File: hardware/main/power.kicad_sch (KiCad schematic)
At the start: 34 parts, among them Q1 SSM3J338R, Q10 SSM3J338R, Q2 BCP53, Q3 SSM3J338R, Q4 BC817, Q5 SSM3J338R, Q6 BC807, Q7 BC817, Q8 SSM3J338R, U5 AP2114H-3.3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

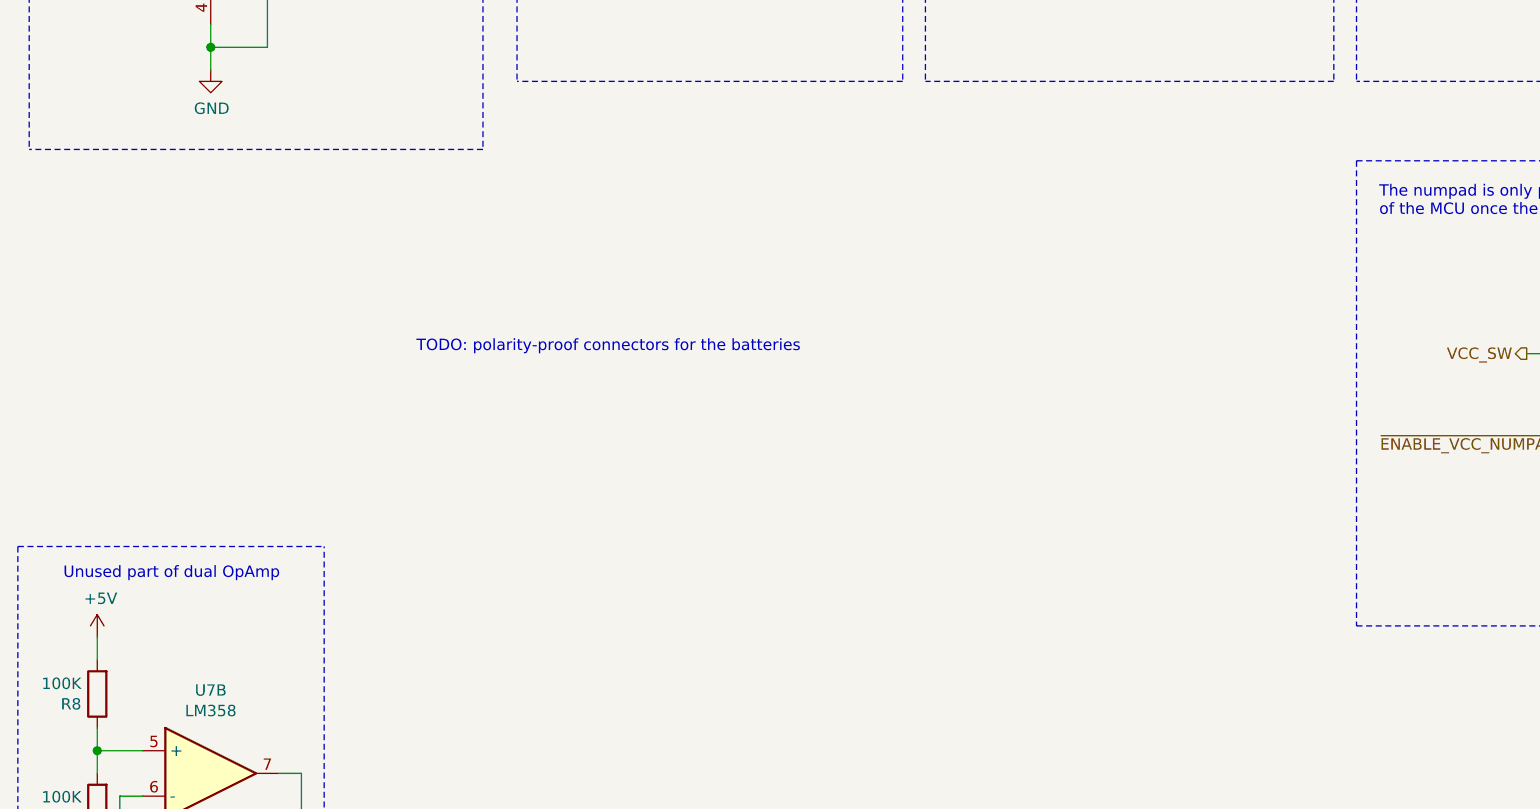
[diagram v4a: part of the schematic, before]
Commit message: Re-add USB voltage sense circuit
Due to firmware limitations the USB voltage cannot be used directly for
waking up the microcontroller.
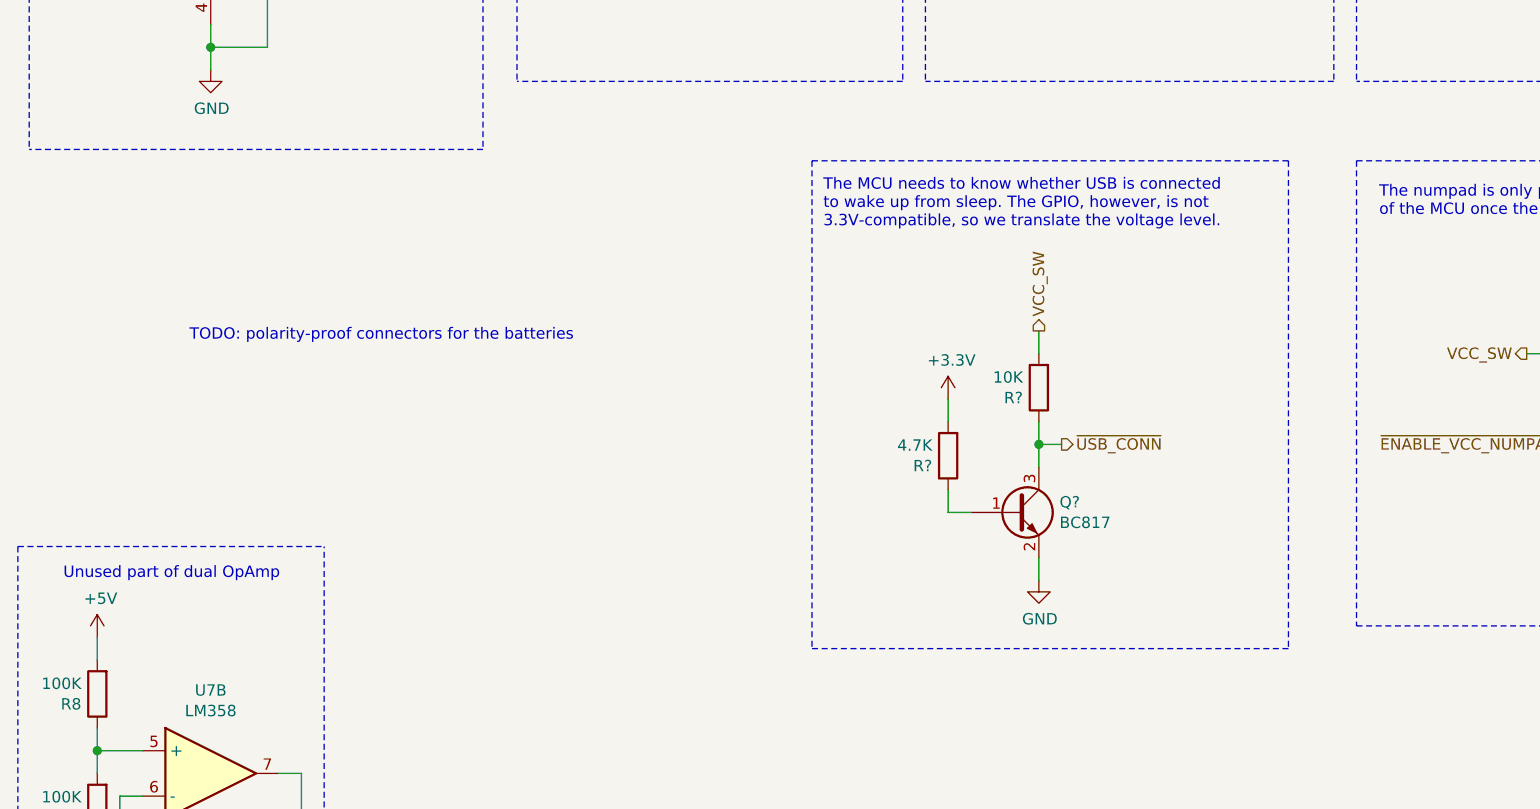
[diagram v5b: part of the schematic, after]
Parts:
- added Q?: BC817, Package_TO_SOT_SMD:SOT-23, symbol Transistor_BJT:BC817
- added R?: 10K, Resistor_SMD:R_0603_1608Metric, symbol Device:R
- added R?: 4.7K, Resistor_SMD:R_0603_1608Metric, symbol Device:R
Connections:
- net +3V3: now also R?.2
- net GND: now also Q?.2 (E)
- net VCC_SW: now also R?.2
- new net: Q?.1 (B), R?.1
- new net ~USB_CONN: Q?.3 (C), R?.1
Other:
- note added: "The MCU needs to know whether USB is connected to wake up from sleep. The GPIO, however, is not 3.3V-compatible, so we translate the voltage level."
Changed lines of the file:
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@@
   (junction (at 74.93 55.88) (diameter 1.016) (color 0 0 0 0))
   (junction (at 97.79 39.37) (diameter 1.016) (color 0 0 0 0))
+  (junction (at 128.27 140.97) (diameter 1.016) (color 0 0 0 0))
   (junction (at 137.16 39.37) (diameter 1.016) (color 0 0 0 0))
   (junction (at 137.16 52.07) (diameter 1.016) (color 0 0 0 0))
@@
     (stroke (width 0) (type solid) (color 0 0 0 0))
   )
+  (wire (pts (xy 118.11 135.89) (xy 118.11 138.43))
+    (stroke (width 0) (type solid) (color 0 0 0 0))
+  )
+  (wire (pts (xy 118.11 146.05) (xy 118.11 148.59))
+    (stroke (width 0) (type solid) (color 0 0 0 0))
+  )
+  (wire (pts (xy 118.11 148.59) (xy 120.65 148.59))
+    (stroke (width 0) (type solid) (color 0 0 0 0))
+  )
   (wire (pts (xy 127 69.85) (xy 127 72.39))
     (stroke (width 0) (type solid) (color 0 0 0 0))
@@
     (stroke (width 0) (type solid) (color 0 0 0 0))
   )
+  (wire (pts (xy 128.27 128.27) (xy 128.27 130.81))
+    (stroke (width 0) (type solid) (color 0 0 0 0))
+  )
+  (wire (pts (xy 128.27 138.43) (xy 128.27 140.97))
+    (stroke (width 0) (type solid) (color 0 0 0 0))
+  )
+  (wire (pts (xy 128.27 140.97) (xy 128.27 143.51))
+    (stroke (width 0) (type solid) (color 0 0 0 0))
+  )
+  (wire (pts (xy 128.27 140.97) (xy 130.81 140.97))
+    (stroke (width 0) (type solid) (color 0 0 0 0))
+  )
+  (wire (pts (xy 128.27 153.67) (xy 128.27 156.21))
+    (stroke (width 0) (type solid) (color 0 0 0 0))
+  )
   (wire (pts (xy 129.54 52.07) (xy 129.54 46.99))
     (stroke (width 0) (type solid) (color 0 0 0 0))
@@
     (stroke (width 0) (type dash) (color 0 0 0 0))
   )
+  (polyline (pts (xy 102.87 109.22) (xy 102.87 163.83))
+    (stroke (width 0) (type dash) (color 0 0 0 0))
+  )
+  (polyline (pts (xy 102.87 109.22) (xy 156.21 109.22))
+    (stroke (width 0) (type dash) (color 0 0 0 0))
+  )
   (polyline (pts (xy 113.03 17.78) (xy 113.03 100.33))
     (stroke (width 0) (type dash) (color 0 0 0 0))
@@
   )
   (polyline (pts (xy 115.57 17.78) (xy 161.29 17.78))
+    (stroke (width 0) (type dash) (color 0 0 0 0))
+  )
+  (polyline (pts (xy 156.21 109.22) (xy 156.21 163.83))
+    (stroke (width 0) (type dash) (color 0 0 0 0))
+  )
+  (polyline (pts (xy 156.21 163.83) (xy 102.87 163.83))
     (stroke (width 0) (type dash) (color 0 0 0 0))
   )
@@
     (effects (font (size 1.27 1.27)) (justify left bottom))
   )
-  (text "TODO: polarity-proof connectors for the batteries" (at 101.6 130.81 180)
+  (text "TODO: polarity-proof connectors for the batteries" (at 76.2 129.54 180)
     (effects (font (size 1.27 1.27)) (justify right bottom))
+  )
+  (text "The MCU needs to know whether USB is connected\nto wake up from sleep. The GPIO, however, is not\n3.3V-compatible, so we translate the voltage level."
+    (at 104.14 116.84 0)
+    (effects (font (size 1.27 1.27)) (justify left bottom))
   )
   (text "A bidirectional switch is required to prevent\ncurrent flowing through the constant curren\nsource during battery operation."
@@
     (effects (font (size 1.27 1.27)) (justify left))
   )
+  (hierarchical_label "VCC_SW" (shape output) (at 128.27 128.27 90)
+    (effects (font (size 1.27 1.27)) (justify left))
+  )
+  (hierarchical_label "~USB_CONN" (shape output) (at 130.81 140.97 0)
+    (effects (font (size 1.27 1.27)) (justify left))
+  )
   (hierarchical_label "~BAL_HIGH" (shape input) (at 177.8 46.99 180)
     (effects (font (size 1.27 1.27)) (justify right))
@@
     )
   )
+  (symbol (lib_id "power:+3.3V") (at 118.11 135.89 0) (unit 1)
+    (in_bom yes) (on_board yes)
+    (property "Reference" "#PWR?" (id 0) (at 118.11 139.7 0)
+      (effects (font (size 1.27 1.27)) hide)
+    )
+    (property "Value" "+3.3V" (id 1) (at 118.4783 131.5656 0))
+    (property "Footprint" "" (id 2) (at 118.11 135.89 0)
+      (effects (font (size 1.27 1.27)) hide)
+    )
+    (property "Datasheet" "" (id 3) (at 118.11 135.89 0)
+      (effects (font (size 1.27 1.27)) hide)
+    )
+  )
   (symbol (lib_id "power:+BATT") (at 210.82 36.83 0) (unit 1)
     (in_bom yes) (on_board yes)
@@
     )
   )
+  (symbol (lib_id "power:GND") (at 128.27 156.21 0) (unit 1)
+    (in_bom yes) (on_board yes)
+    (property "Reference" "#PWR?" (id 0) (at 128.27 162.56 0)
+      (effects (font (size 1.27 1.27)) hide)
+    )
+    (property "Value" "GND" (id 1) (at 128.3843 160.5344 0))
+    (property "Footprint" "" (id 2) (at 128.27 156.21 0)
+      (effects (font (size 1.27 1.27)) hide)
+    )
+    (property "Datasheet" "" (id 3) (at 128.27 156.21 0)
+      (effects (font (size 1.27 1.27)) hide)
+    )
+  )
   (symbol (lib_id "power:GND") (at 190.5 153.67 0) (unit 1)
     (in_bom yes) (on_board yes)
@@
     )
   )
+  (symbol (lib_id "Device:R") (at 118.11 142.24 180) (unit 1)
+    (in_bom yes) (on_board yes)
+    (property "Reference" "R?" (id 0) (at 116.3319 143.3894 0)
+      (effects (font (size 1.27 1.27)) (justify left))
+    )
+    (property "Value" "4.7K" (id 1) (at 116.332 141.091 0)
+      (effects (font (size 1.27 1.27)) (justify left))
+    )
+    (property "Footprint" "Resistor_SMD:R_0603_1608Metric" (id 2) (at 119.888 142.24 90)
+      (effects (font (size 1.27 1.27)) hide)
+    )
+    (property "Datasheet" "~" (id 3) (at 118.11 142.24 0)
+      (effects (font (size 1.27 1.27)) hide)
+    )
+  )
   (symbol (lib_id "Device:R") (at 127 76.2 180) (unit 1)
     (in_bom yes) (on_board yes)
@@
     )
     (property "Datasheet" "~" (id 3) (at 127 76.2 0)
+      (effects (font (size 1.27 1.27)) hide)
+    )
+  )
+  (symbol (lib_id "Device:R") (at 128.27 134.62 180) (unit 1)
+    (in_bom yes) (on_board yes)
+    (property "Reference" "R?" (id 0) (at 126.4919 135.7694 0)
+      (effects (font (size 1.27 1.27)) (justify left))
+    )
+    (property "Value" "10K" (id 1) (at 126.492 133.471 0)
+      (effects (font (size 1.27 1.27)) (justify left))
+    )
+    (property "Footprint" "Resistor_SMD:R_0603_1608Metric" (id 2) (at 130.048 134.62 90)
+      (effects (font (size 1.27 1.27)) hide)
+    )
+    (property "Datasheet" "~" (id 3) (at 128.27 134.62 0)
       (effects (font (size 1.27 1.27)) hide)
     )
@@
     )
   )
+  (symbol (lib_id "Transistor_BJT:BC817") (at 125.73 148.59 0) (unit 1)
+    (in_bom yes) (on_board yes)
+    (property "Reference" "Q?" (id 0) (at 130.5815 147.4406 0)
+      (effects (font (size 1.27 1.27)) (justify left))
+    )
+    (property "Value" "BC817" (id 1) (at 130.5815 149.7393 0)
+      (effects (font (size 1.27 1.27)) (justify left))
+    )
+    (property "Footprint" "Package_TO_SOT_SMD:SOT-23" (id 2) (at 130.81 150.495 0)
+      (effects (font (size 1.27 1.27) italic) (justify left) hide)
+    )
+    (property "Datasheet" "https://www.onsemi.com/pub/Collateral/BC818-D.pdf" (id 3) (at 125.73 148.59 0)
+      (effects (font (size 1.27 1.27)) (justify left) hide)
+    )
+  )

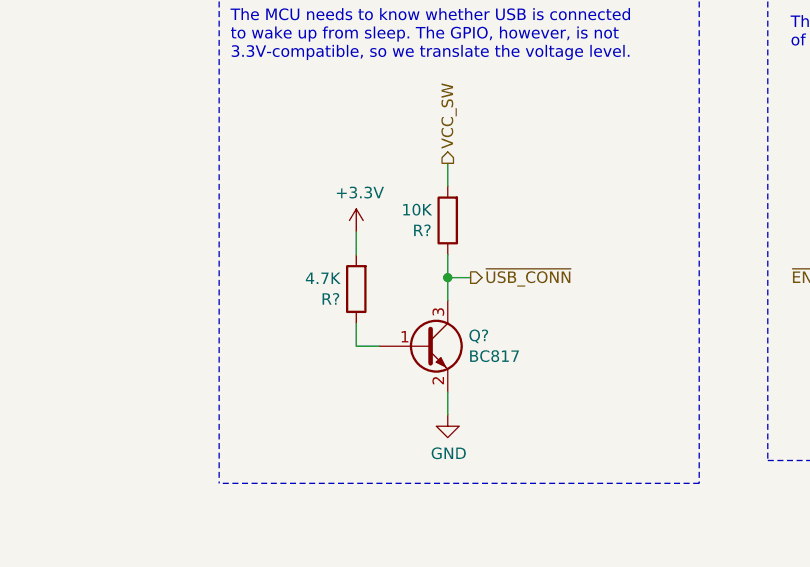
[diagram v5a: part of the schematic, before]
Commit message: Add the USB sense circuit to the PCB
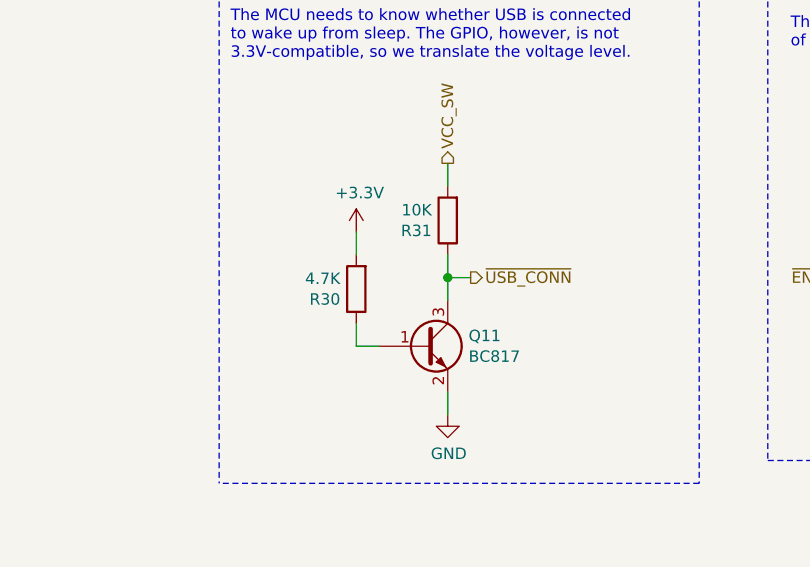
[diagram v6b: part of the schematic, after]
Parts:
- gave numbers to parts that had none: 3
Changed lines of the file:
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@@
   (symbol (lib_id "power:+3.3V") (at 118.11 135.89 0) (unit 1)
     (in_bom yes) (on_board yes)
-    (property "Reference" "#PWR?" (id 0) (at 118.11 139.7 0)
+    (property "Reference" "#PWR0141" (id 0) (at 118.11 139.7 0)
       (effects (font (size 1.27 1.27)) hide)
     )
@@
   (symbol (lib_id "power:GND") (at 128.27 156.21 0) (unit 1)
     (in_bom yes) (on_board yes)
-    (property "Reference" "#PWR?" (id 0) (at 128.27 162.56 0)
+    (property "Reference" "#PWR0150" (id 0) (at 128.27 162.56 0)
       (effects (font (size 1.27 1.27)) hide)
     )
@@
   (symbol (lib_id "Device:R") (at 118.11 142.24 180) (unit 1)
     (in_bom yes) (on_board yes)
-    (property "Reference" "R?" (id 0) (at 116.3319 143.3894 0)
+    (property "Reference" "R30" (id 0) (at 116.3319 143.3894 0)
       (effects (font (size 1.27 1.27)) (justify left))
     )
@@
   (symbol (lib_id "Device:R") (at 128.27 134.62 180) (unit 1)
     (in_bom yes) (on_board yes)
-    (property "Reference" "R?" (id 0) (at 126.4919 135.7694 0)
+    (property "Reference" "R31" (id 0) (at 126.4919 135.7694 0)
       (effects (font (size 1.27 1.27)) (justify left))
     )
@@
   (symbol (lib_id "Transistor_BJT:BC817") (at 125.73 148.59 0) (unit 1)
     (in_bom yes) (on_board yes)
-    (property "Reference" "Q?" (id 0) (at 130.5815 147.4406 0)
-      (effects (font (size 1.27 1.27)) (justify left))
-    )
+    (property "Reference" "Q11" (id 0) (at 130.5815 147.4406 0)
+      (effects (font (size 1.27 1.27)) (justify left))
+    )
